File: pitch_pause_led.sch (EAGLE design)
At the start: 8 parts

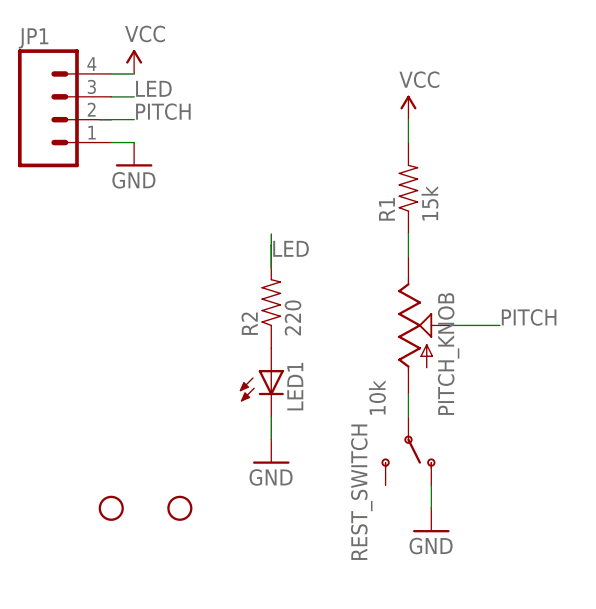
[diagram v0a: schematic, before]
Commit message: through hole led on mini boards
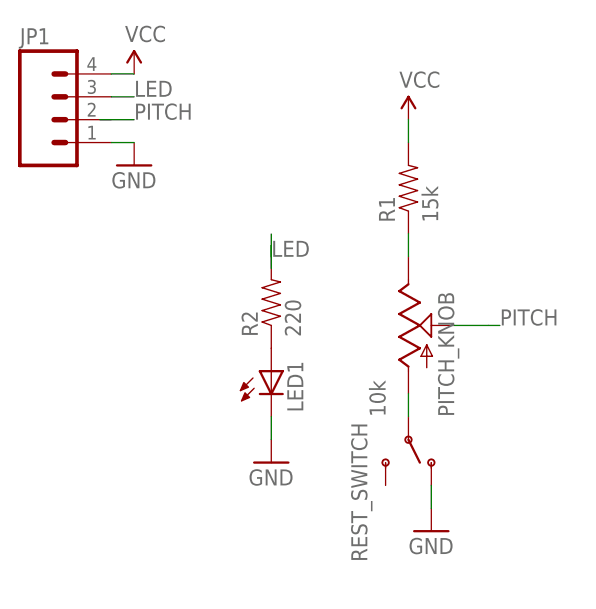
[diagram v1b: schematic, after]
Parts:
- removed STANDOFF1, STANDOFF2: STAND-OFF, SparkFun-Electromechanical:STAND-OFF
- LED1: device LilyPad-Wearables:LED1206 -> SparkFun-LED:LED-3MM-NO_SILK
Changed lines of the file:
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@@
 <part name="SUPPLY1" library="SparkFun-Aesthetics" deviceset="VCC" device=""/>
 <part name="R1" library="SparkFun-Passives" deviceset="RESISTOR" device="AXIAL-0.3" value="15k"/>
-<part name="LED1" library="LilyPad-Wearables" deviceset="LED" device="1206"/>
+<part name="LED1" library="SparkFun-LED" deviceset="LED" device="-3MM-NO_SILK"/>
 <part name="R2" library="SparkFun-Passives" deviceset="RESISTOR" device="AXIAL-0.3" value="220"/>
 <part name="JP1" library="SparkFun-Connectors" deviceset="M04" device="JST-PTH"/>
@@
 <part name="GND2" library="SparkFun-Aesthetics" deviceset="GND" device=""/>
 <part name="GND3" library="SparkFun-Aesthetics" deviceset="GND" device=""/>
-<part name="STANDOFF1" library="SparkFun-Electromechanical" deviceset="STAND-OFF" device=""/>
-<part name="STANDOFF2" library="SparkFun-Electromechanical" deviceset="STAND-OFF" device=""/>
 </parts>
 <sheets>
@@
 <instance part="GND2" gate="1" x="-15.24" y="175.26"/>
 <instance part="GND3" gate="1" x="0" y="142.24"/>
-<instance part="STANDOFF1" gate="G$1" x="-17.78" y="137.16"/>
-<instance part="STANDOFF2" gate="G$1" x="-10.16" y="137.16"/>
 </instances>
 <busses>
